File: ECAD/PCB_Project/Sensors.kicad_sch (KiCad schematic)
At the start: 11 parts, among them J301 Conn_01x03, J302 Conn_01x04, J303 Conn_01x02, J501 Conn_01x04

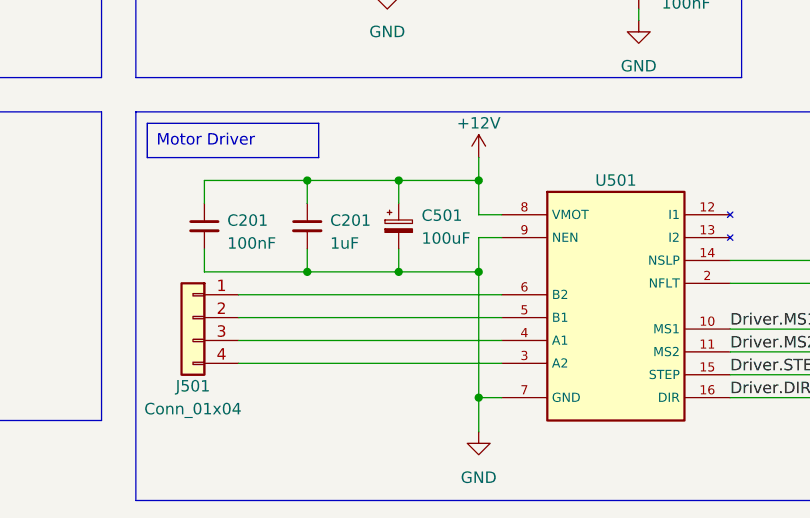
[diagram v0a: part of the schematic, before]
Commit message: Schematic Updates
Wiring up MCU
Adding some footprints
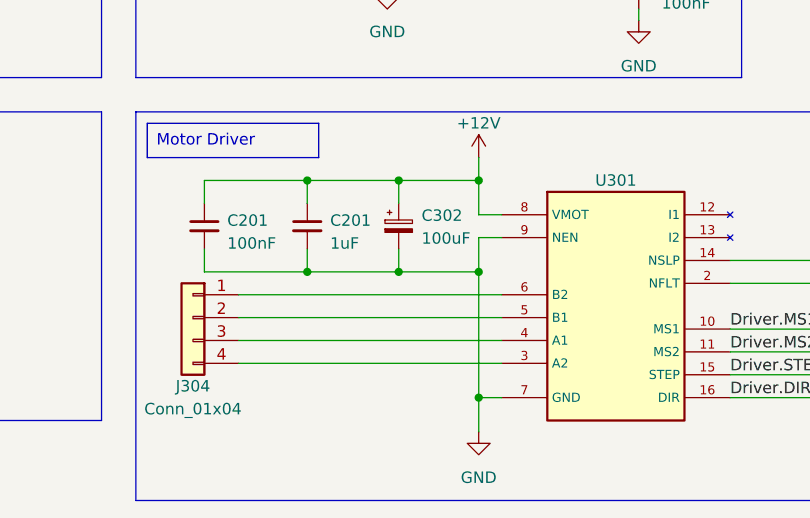
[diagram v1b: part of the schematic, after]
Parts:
- C201: footprint (none) -> Capacitor_THT:C_Disc_D4.3mm_W1.9mm_P5.00mm
- J301: footprint (none) -> Connector_PinHeader_2.54mm:PinHeader_1x03_P2.54mm_Vertical
- J302: footprint (none) -> Connector_PinHeader_2.54mm:PinHeader_1x04_P2.54mm_Vertical
- J303: footprint (none) -> Connector_PinHeader_2.54mm:PinHeader_1x02_P2.54mm_Vertical
- J304: renamed from J501; footprint (none) -> Connector_PinHeader_2.54mm:PinHeader_1x04_P2.54mm_Vertical
- R301, R302: footprint (none) -> Resistor_THT:R_Axial_DIN0204_L3.6mm_D1.6mm_P7.62mm_Horizontal
- renumbered C501 to C302, U501 to U301
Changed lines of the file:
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@@
     (effects (font (size 1.27 1.27)) (justify left top))
   )
-  (label "Driver.MS2" (at 156.21 85.09 0)
+  (label "Driver.MS2" (at 156.21 85.09 0) (fields_autoplaced)
     (effects (font (size 1.27 1.27)) (justify left bottom))
   )
-  (label "Driver.STEP" (at 156.21 87.63 0)
+  (label "Driver.STEP" (at 156.21 87.63 0) (fields_autoplaced)
     (effects (font (size 1.27 1.27)) (justify left bottom))
   )
-  (label "Ultrasonic.Echo" (at 113.03 40.64 0)
+  (label "Ultrasonic.Echo" (at 113.03 40.64 0) (fields_autoplaced)
     (effects (font (size 1.27 1.27)) (justify left bottom))
   )
-  (label "Driver.DIR" (at 156.21 90.17 0)
+  (label "Driver.DIR" (at 156.21 90.17 0) (fields_autoplaced)
     (effects (font (size 1.27 1.27)) (justify left bottom))
   )
-  (label "Ultrasonic.Trigg" (at 113.03 38.1 0)
+  (label "Ultrasonic.Trigg" (at 113.03 38.1 0) (fields_autoplaced)
     (effects (font (size 1.27 1.27)) (justify left bottom))
   )
-  (label "Driver.MS1" (at 156.21 82.55 0)
+  (label "Driver.MS1" (at 156.21 82.55 0) (fields_autoplaced)
     (effects (font (size 1.27 1.27)) (justify left bottom))
   )
@@
       (effects (font (size 1.27 1.27)) (justify left))
     )
-    (property "Footprint" "" (at 97.79 71.12 0)
+    (property "Footprint" "Capacitor_THT:C_Disc_D4.3mm_W1.9mm_P5.00mm" (at 97.79 71.12 0)
       (effects (font (size 1.27 1.27)) hide)
     )
@@
       (effects (font (size 1.27 1.27)))
     )
-    (property "Footprint" "" (at 31.75 36.83 0)
+    (property "Footprint" "Connector_PinHeader_2.54mm:PinHeader_1x03_P2.54mm_Vertical" (at 31.75 36.83 0)
       (effects (font (size 1.27 1.27)) hide)
     )
@@
   (symbol (lib_id "power:+12V") (at 128.27 63.5 0) (unit 1)
     (in_bom yes) (on_board yes) (dnp no) (fields_autoplaced)
-    (property "Reference" "#PWR0503" (at 128.27 67.31 0)
+    (property "Reference" "#PWR0307" (at 128.27 67.31 0)
       (effects (font (size 1.27 1.27)) hide)
     )
@@
   (symbol (lib_id "power:GND") (at 128.27 93.98 0) (unit 1)
     (in_bom yes) (on_board yes) (dnp no) (fields_autoplaced)
-    (property "Reference" "#PWR0502" (at 128.27 100.33 0)
+    (property "Reference" "#PWR0308" (at 128.27 100.33 0)
       (effects (font (size 1.27 1.27)) hide)
     )
@@
   (symbol (lib_id "power:+3V3") (at 168.91 72.39 0) (unit 1)
     (in_bom yes) (on_board yes) (dnp no) (fields_autoplaced)
-    (property "Reference" "#PWR0501" (at 168.91 76.2 0)
+    (property "Reference" "#PWR0309" (at 168.91 76.2 0)
       (effects (font (size 1.27 1.27)) hide)
     )
@@
       (effects (font (size 1.27 1.27)) (justify left))
     )
-    (property "Footprint" "" (at 47.752 40.64 90)
+    (property "Footprint" "Resistor_THT:R_Axial_DIN0204_L3.6mm_D1.6mm_P7.62mm_Horizontal" (at 47.752 40.64 90)
       (effects (font (size 1.27 1.27)) hide)
     )
@@
   (symbol (lib_id "Device:C_Polarized_Small") (at 119.38 71.12 0) (unit 1)
     (in_bom yes) (on_board yes) (dnp no) (fields_autoplaced)
-    (property "Reference" "C501" (at 121.92 69.9389 0)
+    (property "Reference" "C302" (at 121.92 69.9389 0)
       (effects (font (size 1.27 1.27)) (justify left))
     )
@@
       (effects (font (size 1.27 1.27)))
     )
-    (property "Footprint" "" (at 107.95 40.64 0)
+    (property "Footprint" "Connector_PinHeader_2.54mm:PinHeader_1x04_P2.54mm_Vertical" (at 107.95 40.64 0)
       (effects (font (size 1.27 1.27)) hide)
     )
@@
       (effects (font (size 1.27 1.27)) (justify left))
     )
-    (property "Footprint" "" (at 109.22 71.12 0)
+    (property "Footprint" "Capacitor_THT:C_Disc_D4.3mm_W1.9mm_P5.00mm" (at 109.22 71.12 0)
       (effects (font (size 1.27 1.27)) hide)
     )
@@
       (effects (font (size 1.27 1.27)) (justify left))
     )
-    (property "Footprint" "" (at 146.05 44.45 0)
+    (property "Footprint" "Capacitor_THT:C_Disc_D4.3mm_W1.9mm_P5.00mm" (at 146.05 44.45 0)
       (effects (font (size 1.27 1.27)) hide)
     )
@@
   (symbol (lib_id "Connector_Generic:Conn_01x04") (at 96.52 81.28 0) (mirror y) (unit 1)
     (in_bom yes) (on_board yes) (dnp no)
-    (property "Reference" "J501" (at 96.52 88.9 0)
+    (property "Reference" "J304" (at 96.52 88.9 0)
       (effects (font (size 1.27 1.27)))
     )
@@
       (effects (font (size 1.27 1.27)))
     )
-    (property "Footprint" "" (at 96.52 81.28 0)
+    (property "Footprint" "Connector_PinHeader_2.54mm:PinHeader_1x04_P2.54mm_Vertical" (at 96.52 81.28 0)
       (effects (font (size 1.27 1.27)) hide)
     )
@@
       (effects (font (size 1.27 1.27)))
     )
-    (property "Footprint" "" (at 31.75 82.55 0)
+    (property "Footprint" "Connector_PinHeader_2.54mm:PinHeader_1x02_P2.54mm_Vertical" (at 31.75 82.55 0)
       (effects (font (size 1.27 1.27)) hide)
     )
@@
       (effects (font (size 1.27 1.27)) (justify left))
     )
-    (property "Footprint" "" (at 41.402 74.93 90)
+    (property "Footprint" "Resistor_THT:R_Axial_DIN0204_L3.6mm_D1.6mm_P7.62mm_Horizontal" (at 41.402 74.93 90)
       (effects (font (size 1.27 1.27)) hide)
     )
@@
   (symbol (lib_id "318_Part_Library:MP6500") (at 143.51 64.77 0) (unit 1)
     (in_bom yes) (on_board yes) (dnp no) (fields_autoplaced)
-    (property "Reference" "U501" (at 143.51 66.04 0)
-      (effects (font (size 1.27 1.27)))
-    )
+    (property "Reference" "U301" (at 143.51 66.04 0)
+      (effects (font (size 1.27 1.27)))
+    )

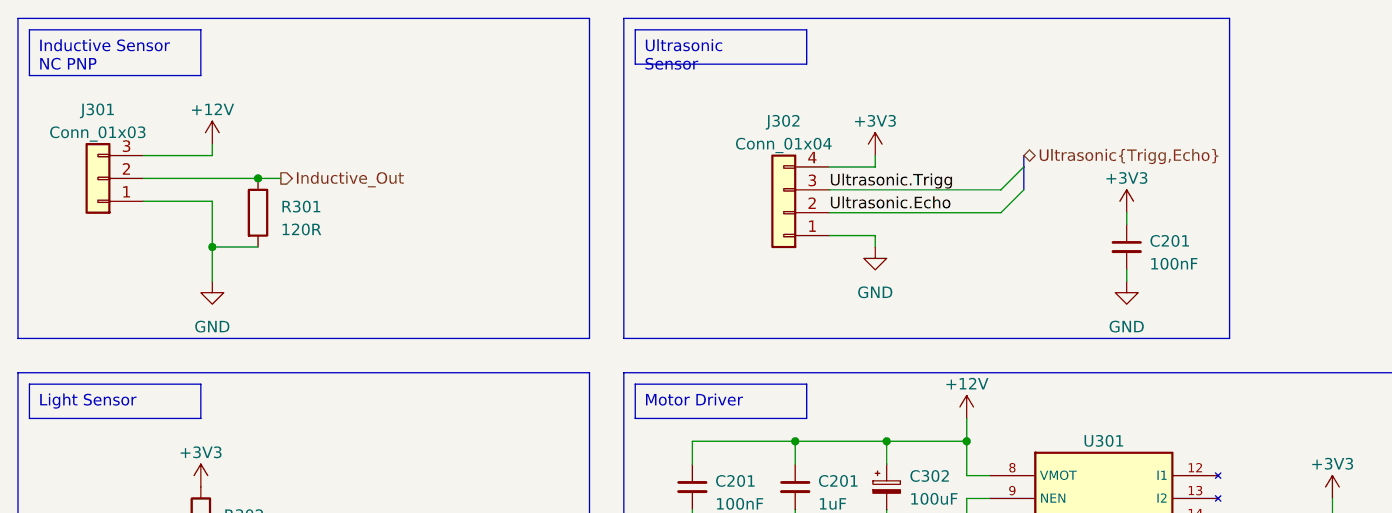
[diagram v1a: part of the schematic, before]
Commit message: Adding Inductive Sensor Transistor
Sims + Schematics
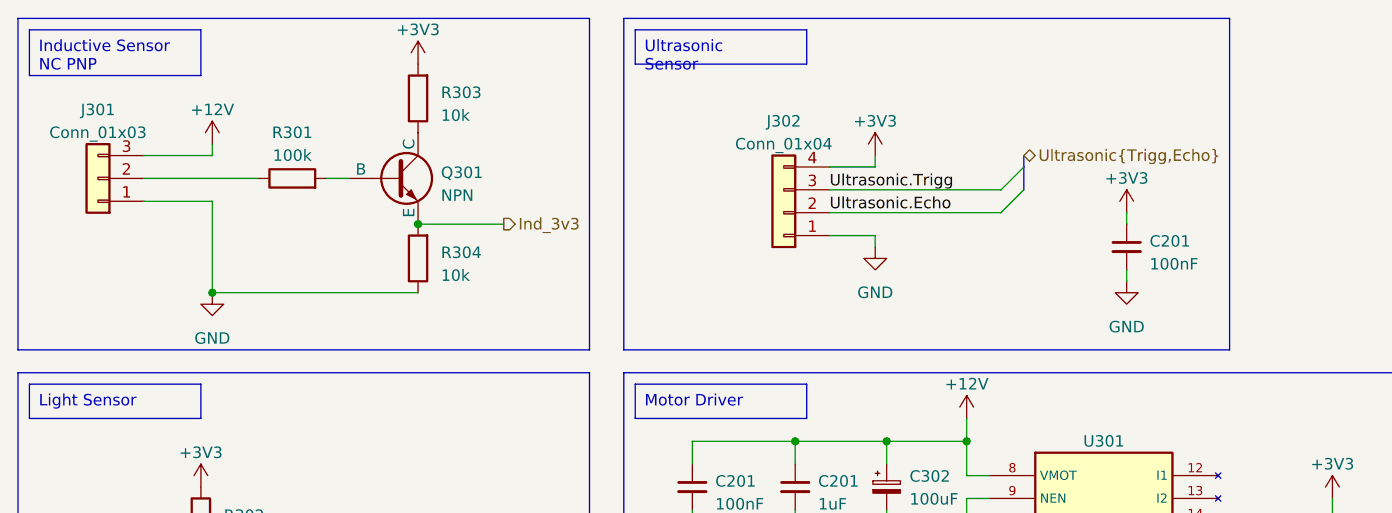
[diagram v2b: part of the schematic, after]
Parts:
- added Q301: NPN, symbol Simulation_SPICE:NPN
- added R303, R304: 10k, symbol Device:R
- R301: value 120R -> 100k; footprint Resistor_THT:R_Axial_DIN0204_L3.6mm_D1.6mm_P7.62mm_Horizontal -> (none)
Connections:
- net +3V3: now also R303.2
- net GND: now also R304.1; no longer R301.2
- net Inductive_Out: no longer names the net of J301.2 (Pin_2), R301.1
- new net: Q301.1 (C), R303.1
- new net: Q301.2 (B), R301.2
- new net Ind_3v3: Q301.3 (E), R304.2

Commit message: First PCB Draft
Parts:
- added J305: Conn_01x03, Connector_PinHeader_2.54mm:PinHeader_1x03_P2.54mm_Vertical, symbol Connector_Generic:Conn_01x03
- C302: footprint (none) -> Capacitor_THT:C_Disc_D4.3mm_W1.9mm_P5.00mm
- Q301: footprint (none) -> Package_TO_SOT_THT:TO-92S_Wide
- R301, R303, R304: footprint (none) -> Resistor_THT:R_Axial_DIN0204_L3.6mm_D1.6mm_P7.62mm_Horizontal
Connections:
- net +3V3: now also Q301.1 (C); no longer R303.2
- net GND: now also J305.1 (Pin_1)
- net Ind_3v3: now also R303.1; no longer Q301.3 (E), R304.2
- new net: Q301.3 (E), R303.2, R304.2
- new net +5V: J305.2 (Pin_2)
- new net SG90_PWM: J305.3 (Pin_3)
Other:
- note added: "Black"
- note added: "Blue"
- note added: "Brown"
- moved on the sheet: Q301, R301, R304

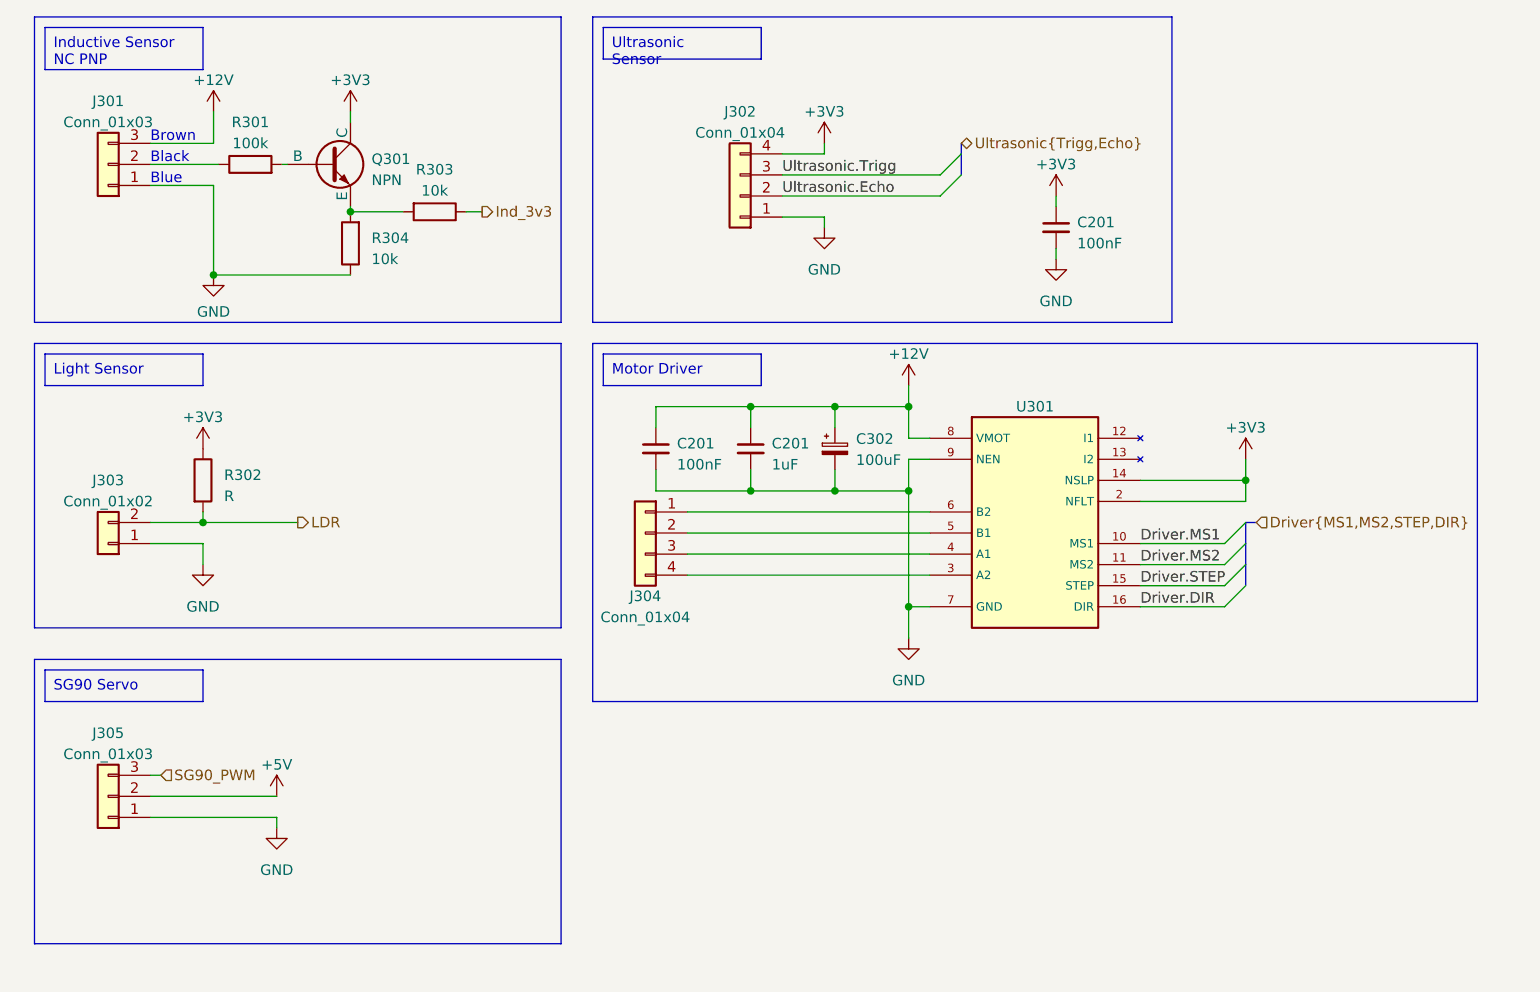
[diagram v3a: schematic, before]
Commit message: PCB Overhaul
Stripboard Expansion
-created
-schematic
-routing

Main PCB
-Flipped sides to not cover buttons
-Started Rerouting
-Changed schematic to accomodate stripboard expansion
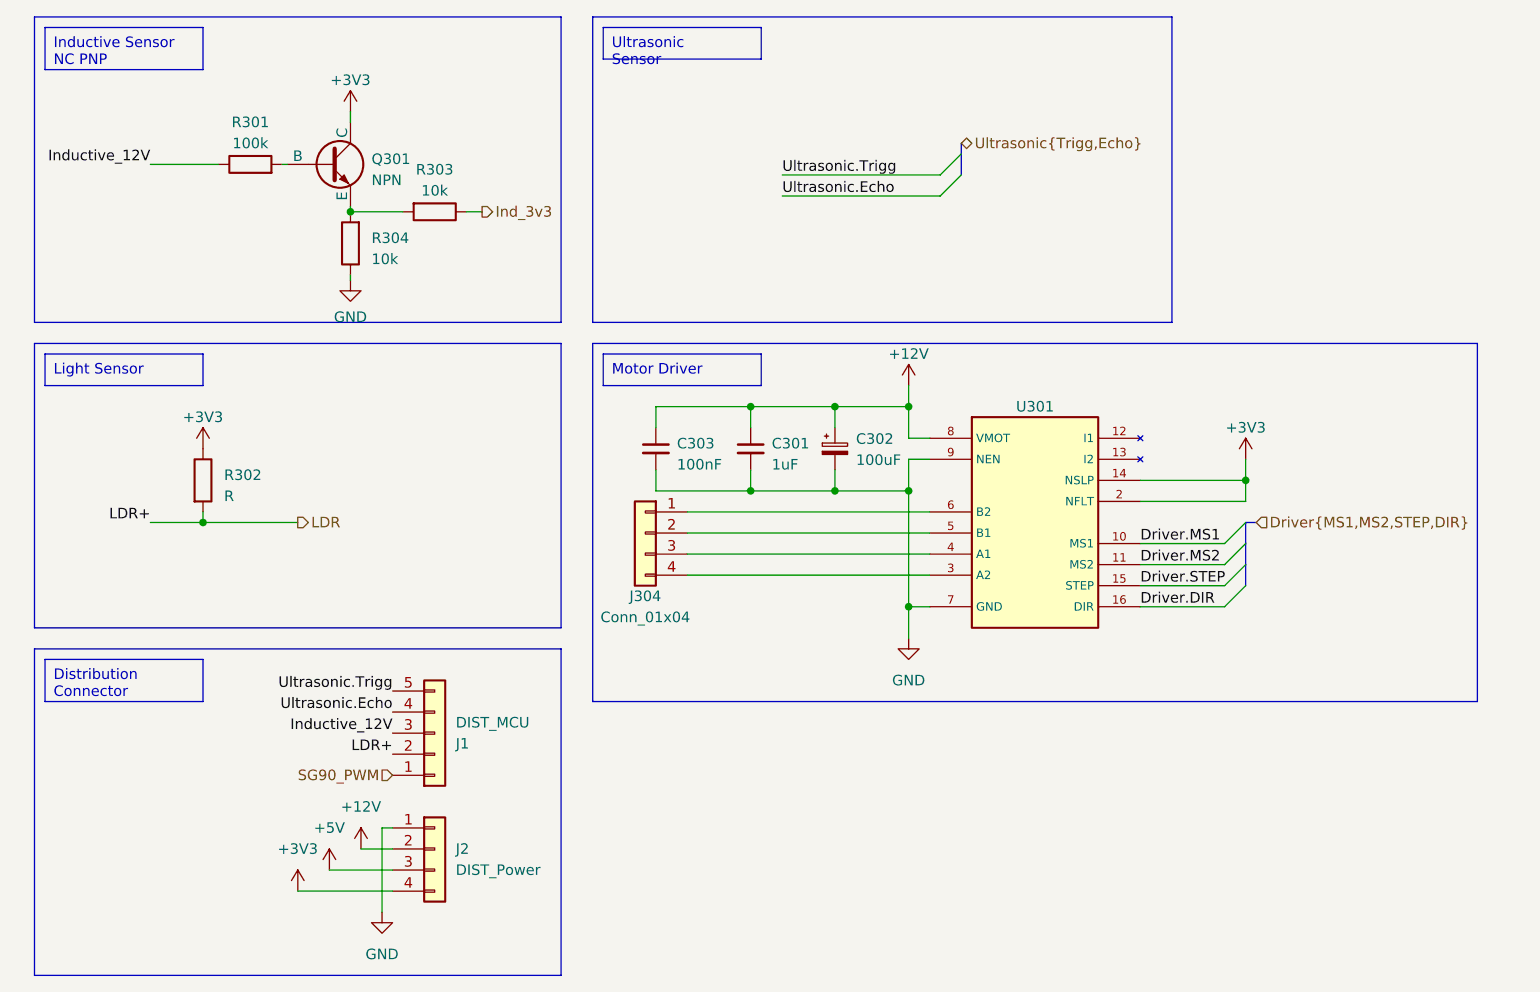
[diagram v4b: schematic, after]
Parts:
- removed C201: 100nF, Capacitor_THT:C_Disc_D4.3mm_W1.9mm_P5.00mm, symbol Device:C_Small
- removed J301, J305: Conn_01x03, Connector_PinHeader_2.54mm:PinHeader_1x03_P2.54mm_Vertical, symbol Connector_Generic:Conn_01x03
- removed J302: Conn_01x04, Connector_PinHeader_2.54mm:PinHeader_1x04_P2.54mm_Vertical, symbol Connector_Generic:Conn_01x04
- removed J303: Conn_01x02, Connector_PinHeader_2.54mm:PinHeader_1x02_P2.54mm_Vertical, symbol Connector_Generic:Conn_01x02
- added J1: DIST_MCU, Connector_PinSocket_2.54mm:PinSocket_1x05_P2.54mm_Vertical, symbol Connector_Generic:Conn_01x05
- added J2: DIST_Power, Connector_PinHeader_2.54mm:PinHeader_1x04_P2.54mm_Vertical, symbol Connector_Generic:Conn_01x04
- renumbered C201 to C301, C201 to C303
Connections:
- net +12V: now also J2.2 (Pin_2)
- net +3V3: now also J2.4 (Pin_4)
- net +5V: now also J2.3 (Pin_3)
- net GND: now also J2.1 (Pin_1)
- net LDR: now also J1.2 (Pin_2)
- net SG90_PWM: now also J1.1 (Pin_1)
- net Ultrasonic.Echo: now also J1.4 (Pin_4)
- net Ultrasonic.Trigg: now also J1.5 (Pin_5)
- net Inductive_12V: now reaches R301.1
- net Inductive_12V: now also J1.3 (Pin_3)
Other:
- note removed: "Black"
- note removed: "Blue"
- note removed: "Brown"

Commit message: Final PCB
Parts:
- removed U301: ~, 318_Footprint_Library:MP6500, symbol 318_Part_Library:MP6500
- added J3: 12V, TerminalBlock:TerminalBlock_bornier-2_P5.08mm, symbol Connector:Screw_Terminal_01x02
- added JP1, JP2: Jumper_2_Open, Resistor_SMD:R_1206_3216Metric, symbol Jumper:Jumper_2_Open
- added U1: ~, 318_Footprint_Library:MP6500, symbol 318_Part_Library:MP6500
- J304: value Conn_01x04 -> STEPPER; footprint Connector_PinHeader_2.54mm:PinHeader_1x04_P2.54mm_Vertical -> TerminalBlock:TerminalBlock_bornier-4_P5.08mm
- R301, R302, R303, R304: footprint Resistor_THT:R_Axial_DIN0204_L3.6mm_D1.6mm_P7.62mm_Horizontal -> Resistor_SMD:R_1206_3216Metric
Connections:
- net +12V: now also J3.1 (Pin_1), U1.8 (VMOT)
- net +3V3: now also JP1.2 (B), JP2.2 (B), U1.2 (NFLT)
- net Driver.DIR: now also U1.16 (DIR)
- net Driver.STEP: now also U1.15 (STEP)
- net GND: now also U1.1 (GND); no longer C301.2, C302.2, C303.2
- net Inductive_12V: now also J1.2 (Pin_2); no longer J1.3 (Pin_3)
- net LDR: now also J1.1 (Pin_1); no longer J1.2 (Pin_2)
- net SG90_PWM: now also J1.4 (Pin_4); no longer J1.1 (Pin_1)
- net Ultrasonic.Echo: now also J1.3 (Pin_3); no longer J1.4 (Pin_4)
- net at J304.1 (Pin_1): now also U1.6 (B2)
- net at J304.2 (Pin_2): now also U1.5 (B1)
- net at J304.3 (Pin_3): now also U1.4 (A1)
- net at J304.4 (Pin_4): now also U1.3 (A2)
- new net: JP2.1 (A), U1.10 (MS1)
- new net: JP1.1 (A), U1.11 (MS2)
- new net: U1.13 (I2), U1.14 (NSLP)
- new net MGND: C301.2, C302.2, C303.2, J3.2 (Pin_2), U1.7 (MGND)
- no-connect marks 0 -> 2
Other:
- moved on the sheet: C301, C302, C303, J304

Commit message: Pushing
COde changes:
MP driver under development
SG90 as well

PCB:
final version, as sent to manufacture

Sims
New sims for report.
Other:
- company: (none) -> Group 9
- title: (none) -> EE318 - Slam Dunk Your Junk
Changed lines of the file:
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@@
 	(generator_version "8.0")
 	(paper "A5")
+	(title_block
+		(title "EE318 - Slam Dunk Your Junk")
+		(date "2024-05-01")
+		(rev "V1")
+		(company "Group 9")
+		(comment 1 "Manufactured Design")
+	)
 	(junction
 		(at 109.22 72.39)
